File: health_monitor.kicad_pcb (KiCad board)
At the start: 4 copper layers, 40 x 40 mm, 65 parts, among them J1 USBC, J2 BAT+_PAD, J3 THERMISTOR, J4 JTAG_HEADER, J5 RFP_PAD, J6 RFN_PAD, U1 MAX86140ENP+T, U2 ADXL366BCCZ-RL7, U3 MAX77972EWX+T, U4 MAX77642ANA+T

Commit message: schematic mostly finished
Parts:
- removed C33, C36: 1uF, Capacitor_SMD:C_0201_0603Metric
- removed C34: 10nF, Capacitor_SMD:C_01005_0402Metric
- removed C35, C38: 22uF, Capacitor_SMD:C_0402_1005Metric
- removed C37: 10uF, Capacitor_SMD:C_0402_1005Metric
- removed J4: JTAG_HEADER, Connector_PinHeader_2.54mm:PinHeader_1x06_P2.54mm_Vertical
- removed J5: RFP_PAD, Connector_PinHeader_2.54mm:PinHeader_1x01_P2.54mm_Vertical
- removed J6: RFN_PAD, Connector_PinHeader_2.54mm:PinHeader_1x01_P2.54mm_Vertical
- added AE1: Antenna, RF_Antenna:Johanson_2450AT18x100, F.Cu at (153.4, 68.4)
- added L4: 2.7nH, Inductor_SMD:L_0402_1005Metric, F.Cu at (147.1, 68.9)
- added R10: 50, Resistor_SMD:R_0201_0603Metric, F.Cu at (122.2, 39.0)
- added R11: 10k, Resistor_SMD:R_0201_0603Metric, F.Cu at (132.4, 43.0)
- added R13: 10k, Resistor_SMD:R_0201_0603Metric, F.Cu at (132.4, 42.2)
- added U5: BQ27427YZFR, Project-Symbols:BQ27427, F.Cu at (130.4, 42.0)
- C15, C16, C18: moved to B.Cu
- C17: footprint Capacitor_SMD:C_0402_1005Metric -> Capacitor_SMD:C_01005_0402Metric; moved to B.Cu
- C22: value 10uF -> 2.2uF; footprint Capacitor_SMD:C_0402_1005Metric -> Capacitor_SMD:C_0201_0603Metric
- C23, C24: value 2.2uF -> 1uF
- C26: value 100nF -> 47pF
- C27: value 2.2uF -> 10uF
- C28: value 10uF -> 47pF; footprint Capacitor_SMD:C_0402_1005Metric -> Capacitor_SMD:C_01005_0402Metric
- C29: footprint Capacitor_SMD:C_0402_1005Metric -> Capacitor_SMD:C_0201_0603Metric
- C30: value 40uF -> 4.7uF; footprint Capacitor_SMD:C_0805_2012Metric -> Capacitor_SMD:C_0201_0603Metric
- C31: value 40uF -> 2.2uF; footprint Capacitor_SMD:C_0805_2012Metric -> Capacitor_SMD:C_0201_0603Metric
- C32: value 40uF -> 1pF; footprint Capacitor_SMD:C_0805_2012Metric -> Capacitor_SMD:C_0402_1005Metric
- J2: value BAT+_PAD -> Conn_01x02_Pin; footprint Connector_PinHeader_2.54mm:PinHeader_1x01_P2.54mm_Vertical -> Connector_PinHeader_2.54mm:PinHeader_1x02_P2.54mm_Vertical
- J3: value THERMISTOR -> Conn_01x05; footprint Connector_PinHeader_2.54mm:PinHeader_1x02_P2.54mm_Vertical -> Connector_PinHeader_2.54mm:PinHeader_1x05_P2.54mm_Vertical
- L1: value 6.8uH -> 2.2uH; footprint Inductor_SMD:L_Pulse_PA4332 -> Inductor_SMD:L_1008_2520Metric
- L2: value 1uF -> 2.2uH; footprint Inductor_SMD:L_0805_2012Metric -> Inductor_SMD:L_1008_2520Metric
- L3: value 2.2uH -> 3.9nH; footprint Inductor_SMD:L_1210_3225Metric -> Inductor_SMD:L_0402_1005Metric
- R1: footprint Resistor_SMD:R_0603_1608Metric -> Resistor_SMD:R_0402_1005Metric_Pad0.72x0.64mm_HandSolder
- R12: value 0 -> 300k; footprint Resistor_SMD:R_0603_1608Metric -> Resistor_SMD:R_0201_0603Metric
- R2: value 14k -> 680k; footprint Resistor_SMD:R_0603_1608Metric -> Resistor_SMD:R_0402_1005Metric_Pad0.72x0.64mm_HandSolder
- R3: value 133k -> 150k; footprint Resistor_SMD:R_0603_1608Metric -> Resistor_SMD:R_0402_1005Metric_Pad0.72x0.64mm_HandSolder
- R4: value 28k -> 350k; footprint Resistor_SMD:R_0603_1608Metric -> Resistor_SMD:R_0402_1005Metric_Pad0.72x0.64mm_HandSolder
- R5: value 56.2k -> 150k; footprint Resistor_SMD:R_0603_1608Metric -> Resistor_SMD:R_0402_1005Metric_Pad0.72x0.64mm_HandSolder
- R6: value 80.6k -> 240k; footprint Resistor_SMD:R_0603_1608Metric -> Resistor_SMD:R_0201_0603Metric
- R7: footprint Resistor_SMD:R_0603_1608Metric -> Resistor_SMD:R_0201_0603Metric
- R8: value 10m -> 27.4k; footprint Resistor_SMD:R_0603_1608Metric -> Resistor_SMD:R_0201_0603Metric
- R9: value 10k -> 1k; footprint Resistor_SMD:R_0603_1608Metric -> Resistor_SMD:R_0201_0603Metric
- U3: value MAX77972EWX+T -> BQ25176JDSGR; footprint Project-Symbols:MAX77972EWX+T -> Project-Symbols:BQ25176
- U4: value MAX77642ANA+T -> TPS650531RGER; footprint Project-Symbols:MAX77642ANA+T -> Project-Symbols:TPS650531
- moved L2 92.6 mm to (141.7, 42.7)
- moved C27 86.3 mm to (135.7, 39.7)
- moved C29 83.7 mm to (143.6, 44.9), turned to 180 degrees
- moved R5 80.9 mm to (141.6, 45.5), turned to -90 degrees
- moved R4 79.4 mm to (143.4, 46.7)
- moved C30 79.2 mm to (140.7, 52.3), turned to 90 degrees
- moved C31 78.2 mm to (136.8, 51.8)
- moved L3 77.9 mm to (149.1, 68.4)
- moved C32 77.7 mm to (145.1, 68.4)
- moved R6 76.1 mm to (138.4, 51.6), turned to -90 degrees
- moved R3 73.0 mm to (135.1, 45.2), turned to 180 degrees
- moved R12 72.6 mm to (139.6, 51.2), turned to 180 degrees
- moved R2 72.2 mm to (134.5, 43.3), turned to 90 degrees
- moved C22 71.5 mm to (128.4, 42.4)
- moved R8 71.4 mm to (127.7, 39.0), turned to 90 degrees
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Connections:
- C1 pad 1: /V_{D} -> /V_{2.0}
- C2 pad 1: /V_{D} -> /V_{2.0}
- C22 pad 1: /Power Management ICs/BAT+ -> GNDREF
- C22 pad 2: GNDREF -> Net-(U5-VDD)
- C23 pad 1: /V_{BUS} -> /Power Management ICs/BAT+
- C24 pad 1: Net-(U3-VDD) -> GNDREF
- C24 pad 2: GNDREF -> /Power Management ICs/V_{BAT}
- C25 pad 2: Net-(U3-PVL) -> /Power Management ICs/V_{BAT}
- C26 pad 1: Net-(U3-BST) -> /V_{LED}
- C26 pad 2: Net-(C26-Pad2) -> Net-(U4-FB_DCDC1)
- C27 pad 1: /Power Management ICs/BAT+ -> /V_{LED}
- C28 pad 1: /Power Management ICs/CHG_OUT -> /V_{2.0}
- C28 pad 2: GNDREF -> Net-(U4-FB_DCDC2)
- C29 pad 1: /Power Management ICs/CHG_OUT -> /V_{2.0}
- C3 pad 1: /V_{D} -> /V_{2.0}
- C30 pad 1: /V_{2.0} -> /V_{A}
- C31 pad 1: /V_{D} -> GNDREF
- C31 pad 2: GNDREF -> /V_{2.0}
- C32 pad 1: /V_{LED} -> /CC2674R10/RF_{P}
- C32 pad 2: GNDREF -> Net-(C32-Pad2)
- C4 pad 2: /V_{D} -> /V_{2.0}
- C5 pad 1: /V_{D} -> /V_{2.0}
- J1 pad A5: /CC1 -> unconnected-(J1-CC_{1}-PadA5)
- J1 pad A6: /Power Management ICs/DP -> unconnected-(J1-D_{+}-PadA6)
- J1 pad A7: /Power Management ICs/DN -> unconnected-(J1-D_{-}-PadA7)
- J1 pad B5: /CC2 -> unconnected-(J1-CC_{2}-PadB5)
- J1 pad B6: /Power Management ICs/DP -> unconnected-(J1-D_{+}-PadB6)
- J1 pad B7: /Power Management ICs/DN -> unconnected-(J1-D_{-}-PadB7)
- J3 pad 1: /Power Management ICs/THM+ -> /CC2674R10/JTAG_{TCKC}
- J3 pad 2: GNDREF -> /CC2674R10/JTAG_{TMSC}
- L1 pad 1: Net-(MCU1A-VDDR) -> Net-(U4-L1)
- L1 pad 2: Net-(MCU1A-DCDC_SW) -> /V_{LED}
- L2 pad 1: Net-(C26-Pad2) -> Net-(U4-L2)
- L2 pad 2: /Power Management ICs/CHG_OUT -> /V_{2.0}
- L3 pad 1: Net-(U4A-LXA) -> Net-(C32-Pad2)
- L3 pad 2: Net-(C34-Pad1) -> Net-(AE1-A)
- MCU1 pad 13: /V_{D} -> /V_{2.0}
- MCU1 pad 22: /V_{D} -> /V_{2.0}
- MCU1 pad 33: Net-(MCU1A-DCDC_SW) -> unconnected-(MCU1A-DCDC_SW-Pad33)
- MCU1 pad 34: /V_{D} -> /V_{2.0}
- MCU1 pad 44: /V_{D} -> /V_{2.0}
- R1 pad 1: /V_{D} -> /V_{2.0}
- R12 pad 1: Net-(U4A-EN0) -> GNDREF
- R12 pad 2: /Power Management ICs/CHG_OUT -> Net-(U4-FB_LDO1)
- R2 pad 1: GNDREF -> Net-(U4-FB_DCDC1)
- R2 pad 2: Net-(U4A-RSET_IPK) -> /V_{LED}
- R3 pad 2: Net-(U4A-RSET_SBB2) -> Net-(U4-FB_DCDC1)
- R4 pad 1: GNDREF -> Net-(U4-FB_DCDC2)
- R4 pad 2: Net-(U4A-RSET_SBB1) -> /V_{2.0}
- R5 pad 2: Net-(U4A-RSET_SBB0) -> Net-(U4-FB_DCDC2)
- R6 pad 1: GNDREF -> Net-(U4-FB_LDO1)
- R6 pad 2: Net-(U4A-RSET_LDO) -> /V_{A}
- R7 pad 1: /CHG_EN -> GNDREF
- R7 pad 2: GNDREF -> Net-(U3-BIAS)
- R8 pad 1: Net-(U3-CSP) -> GNDREF
- R8 pad 2: /Power Management ICs/BAT+ -> Net-(U3-VSET)
- R9 pad 1: /V_{D} -> GNDREF
- R9 pad 2: /CHG_INT -> Net-(R10-Pad1)
- U1 pad A2: /MCU_DIO6 -> /MCU_DIO7
- U1 pad A3: /MCU_DIO7 -> /MCU_DIO6
- U1 pad A4: /MCU_DIO8 -> /MCU_DIO5
- U1 pad A5: /MCU_DIO9 -> /MCU_DIO4
- U1 pad B2: /MCU_DIO10 -> /MCU_DIO3
- U1 pad B3: /MCU_DIO11 -> /MAX86140 AFE/GPIO1
- U1 pad B4: /MCU_DIO12 -> /MAX86140 AFE/GPIO2
- U2 pad 1: /MCU_DIO0 -> /MCU_DIO14
- U2 pad 2: /MCU_DIO2 -> /MCU_DIO13
- U2 pad 3: /MCU_DIO1 -> /MCU_DIO12
- U2 pad 4: /MCU_DIO3 -> /MCU_DIO11
- U2 pad 5: /MCU_DIO4 -> /MCU_DIO10
- U2 pad 6: /MCU_DIO5 -> /MCU_DIO9
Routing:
- net /V_{2.0}: track 0.00 -> 60.1 mm, vias 0 -> 9
- net /V_{LED}: track 0.00 -> 39.4 mm, vias 0 -> 6
- net /Power Management ICs/V_{BAT}: track 0.00 -> 37.1 mm, vias 0 -> 6
- net /MCU_DIO19: track 0.00 -> 24.0 mm, vias 0 -> 2
- net /MCU_DIO18: track 0.00 -> 21.7 mm, vias 0 -> 2
- net /V_{BUS}: track 2.28 -> 22.1 mm
- net Net-(MCU1A-VDDR): track 0.00 -> 14.0 mm, vias 0 -> 3
- net /CC2674R10/JTAG_{TCKC}: track 0.00 -> 12.4 mm
- net /MCU_DIO17: track 0.00 -> 11.5 mm
- net /V_{A}: track 0.00 -> 10.8 mm, vias 0 -> 5
- net /CC2674R10/RESET: track 0.00 -> 10.8 mm
- net /MCU_DIO16: track 0.00 -> 10.6 mm
- net /LED_CATHODE2: track 0.00 -> 10.3 mm, vias 0 -> 2
- net /CC2674R10/JTAG_{TMSC}: track 0.00 -> 9.91 mm
- net /LED_CATHODE0: track 0.00 -> 9.19 mm, vias 0 -> 2
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- added copper zone on F.Cu, net GNDREF
- added copper zone on In1.Cu, net GNDREF

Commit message: ready to order
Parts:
- added P1: , , F.Cu at (158.0, 74.0)
- added P2: , , F.Cu at (122.0, 74.0)
- added P3: MountingHole_2.2mm_M2, MountingHole:MountingHole_2.2mm_M2, F.Cu at (158.0, 38.0)
- C15: footprint Capacitor_SMD:C_0201_0603Metric -> Capacitor_SMD:C_0603_1608Metric
- C16, C18: footprint Capacitor_SMD:C_0402_1005Metric -> Capacitor_SMD:C_0603_1608Metric
- C17, C19: footprint Capacitor_SMD:C_01005_0402Metric -> Capacitor_SMD:C_0603_1608Metric
- C27, C29: footprint Capacitor_SMD:C_0201_0603Metric -> Capacitor_SMD:C_0402_1005Metric
- J1: footprint Project-Symbols:CONN16_203615_MOL -> Project-Symbols:MOLEX_USBC_1054500101
- moved C18 1.80 mm to (139.9, 53.9), turned to 180 degrees
- moved C15 1.02 mm to (142.7, 60.6), turned to 90 degrees
- moved C17 0.85 mm to (141.5, 55.6)
- moved J1 0.70 mm to (124.2, 50.3), turned to -90 degrees
- moved C19 0.56 mm to (136.7, 54.5)
- moved C16 0.28 mm to (145.3, 54.4)
- moved C20 0.10 mm to (133.6, 57.0)
- moved C23 0.10 mm to (129.5, 40.4)
- moved C27 0.08 mm to (135.8, 39.7)
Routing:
- net /V_{BUS}: track 22.1 -> 26.7 mm
- net GNDREF: track 13.9 -> 9.74 mm, vias 90 -> 104
- net /MCU_DIO19: track 24.0 -> 22.6 mm
- net /V_{2.0}: track 60.1 -> 59.4 mm
- added copper zone on B.Cu, net GNDREF
- added copper zone on In2.Cu, net GNDREF

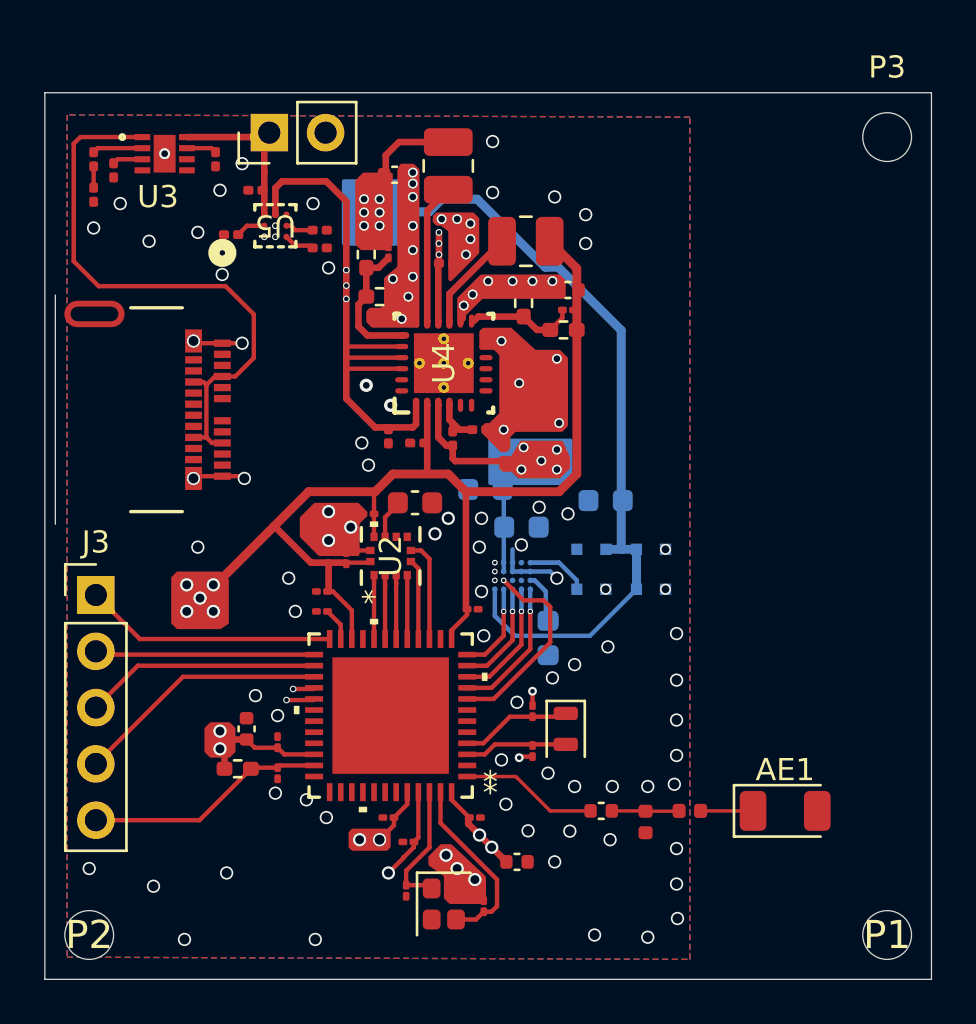
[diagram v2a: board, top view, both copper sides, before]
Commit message: resize to 0603
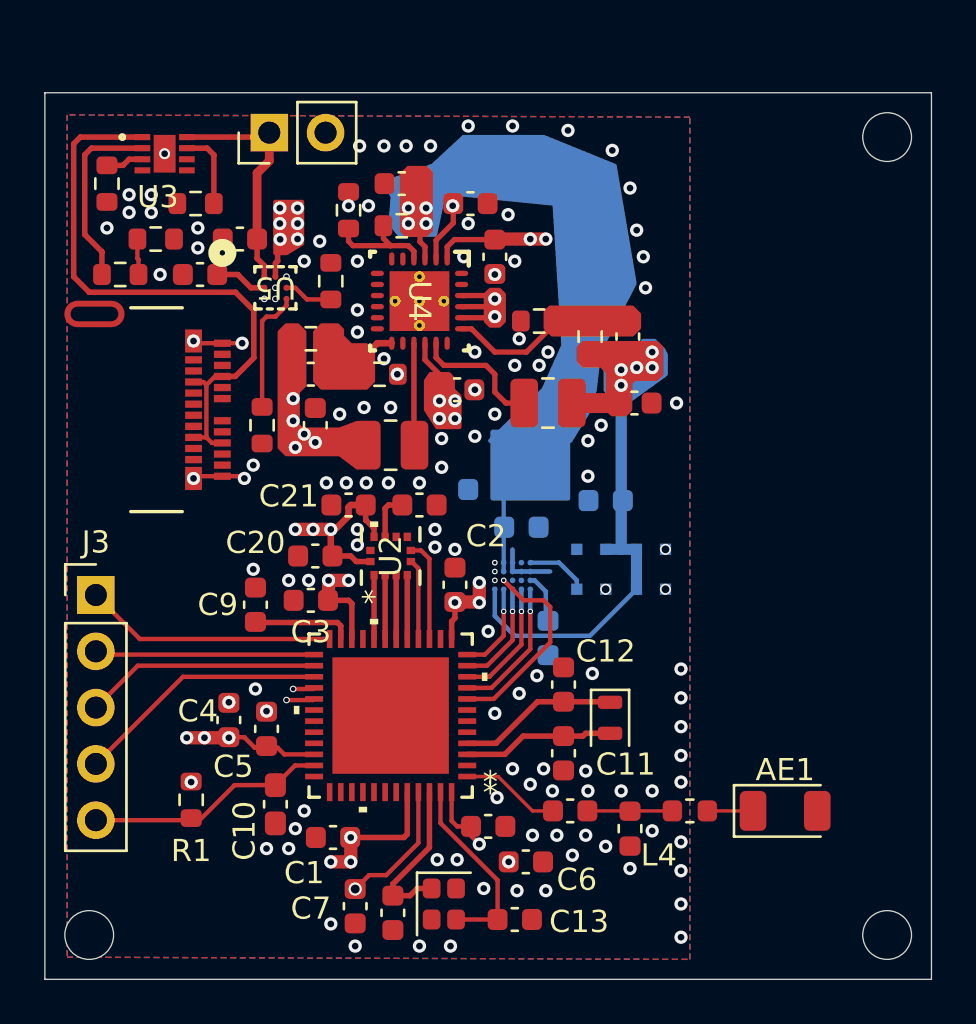
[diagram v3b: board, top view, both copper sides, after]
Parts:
- C1, C11, C12, C13, C14, C2, C20, C21, C26, C28, C3, C5, C7, C8, C9: footprint Capacitor_SMD:C_01005_0402Metric -> Capacitor_SMD:C_0603_1608Metric
- C10: footprint Capacitor_SMD:C_01005_0402Metric -> Capacitor_SMD:C_0603_1608Metric_Pad1.08x0.95mm_HandSolder
- C22, C23, C24, C25, C30, C31: footprint Capacitor_SMD:C_0201_0603Metric -> Capacitor_SMD:C_0603_1608Metric
- C27, C29, C32, C4, C6: footprint Capacitor_SMD:C_0402_1005Metric -> Capacitor_SMD:C_0603_1608Metric
- L3, L4: footprint Inductor_SMD:L_0402_1005Metric -> Inductor_SMD:L_0603_1608Metric
- R1, R2, R3, R4, R5: footprint Resistor_SMD:R_0402_1005Metric_Pad0.72x0.64mm_HandSolder -> Resistor_SMD:R_0603_1608Metric
- R10, R11, R12, R13, R6, R7, R8, R9: footprint Resistor_SMD:R_0201_0603Metric -> Resistor_SMD:R_0603_1608Metric
- moved C27 14.9 mm to (146.6, 50.0)
- moved C30 13.0 mm to (136.1, 40.1), turned to 180 degrees
- moved C29 12.9 mm to (132.2, 51.0), turned to 90 degrees
- moved C28 12.0 mm to (132.0, 48.7), turned to 0 degrees
- moved L1 11.6 mm to (142.7, 50.0), turned to 0 degrees
- moved R12 11.5 mm to (133.7, 41.3), turned to -90 degrees
- moved C26 11.4 mm to (146.3, 47.0), turned to 90 degrees
- moved R4 11.4 mm to (132.0, 47.1), turned to 180 degrees
- moved C31 11.1 mm to (139.2, 41.0), turned to 180 degrees
- moved L2 11.0 mm to (135.6, 51.9), turned to 180 degrees
- moved R2 10.8 mm to (144.6, 47.0), turned to -90 degrees
- moved R6 9.87 mm to (136.1, 42.0), turned to 0 degrees
- moved C24 9.42 mm to (140.3, 43.4)
- moved R11 8.41 mm to (129.8, 51.0), turned to 90 degrees
- moved R3 7.28 mm to (142.3, 46.3), turned to 0 degrees
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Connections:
- U4 pad V1: (no net) -> GNDREF
- U4 pad V2: (no net) -> GNDREF
- U4 pad V3: (no net) -> GNDREF
- U4 pad V4: (no net) -> GNDREF
- U4 pad V5: (no net) -> GNDREF
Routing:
- net /V_{2.0}: track 59.4 -> 32.3 mm, vias 9 -> 21
- net /Power Management ICs/V_{BAT}: track 37.1 -> 14.0 mm, vias 6 -> 14
- net /V_{LED}: track 39.7 -> 22.2 mm, vias 6 -> 5
- net Net-(U3-ISET): track 2.27 -> 8.55 mm
- net Net-(U5-GPOUT): track 1.35 -> 5.56 mm
- net /V_{A}: track 10.8 -> 7.11 mm, vias 5 -> 4
- net Net-(MCU1A-VDDR): track 14.0 -> 17.4 mm
- net Net-(U4-FB_DCDC2): track 4.91 -> 1.50 mm
- net /Power Management ICs/BAT+: track 7.59 -> 11.0 mm
- net Net-(MCU1A-DCOUPL): track 1.49 -> 4.52 mm
- net /MCU_DIO19: track 22.6 -> 19.8 mm
- net /MCU_DIO18: track 21.7 -> 18.9 mm
- net Net-(U4-FB_LDO1): track 2.45 -> 5.10 mm
- net GNDREF: track 9.74 -> 7.31 mm, vias 104 -> 118
- net Net-(MCU1A-K32X_Q2): track 5.00 -> 7.23 mm
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- added copper zone on In2.Cu, net /V_{2.0}
